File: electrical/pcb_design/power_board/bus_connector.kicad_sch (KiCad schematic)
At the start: 6 parts, among them J601 504050-1291, J603 504050-1091

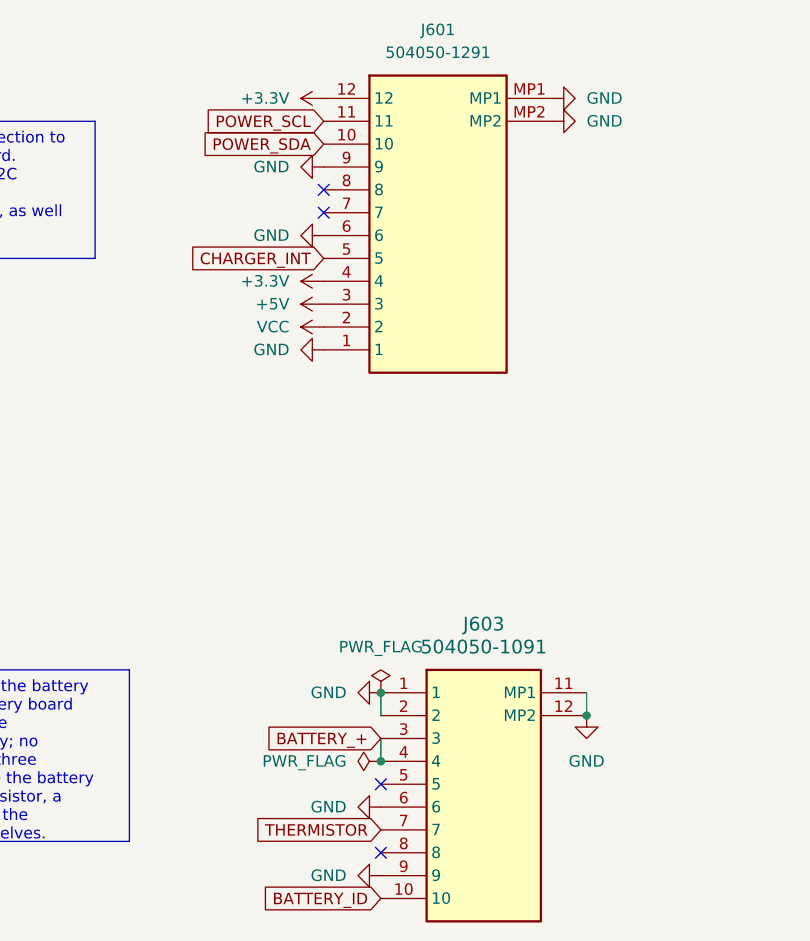
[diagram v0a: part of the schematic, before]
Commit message: Fixed major bug where header orientations need to be swapped on different ends of the cabling.
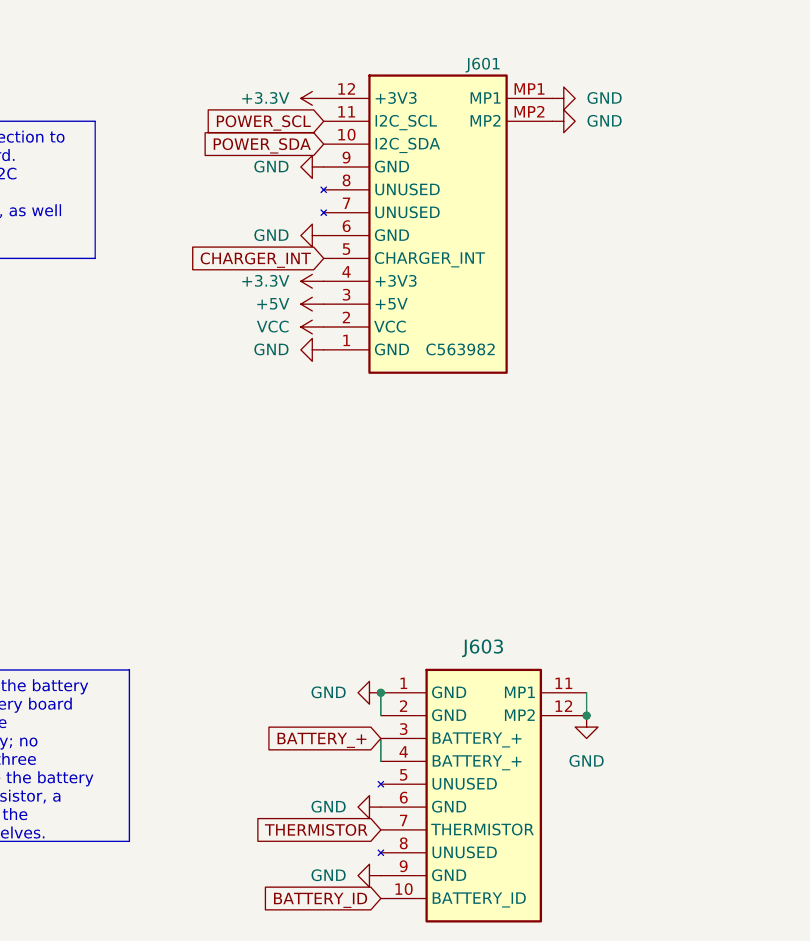
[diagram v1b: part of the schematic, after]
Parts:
- J601: value 504050-1291 -> Interconnect_Power_CPU-Power_side; symbol Molex 504050-1291:504050-1291 -> TVSC:Interconnect_Power_CPU-Power_side; Height 2.15 -> (none); Manufacturer MOLEX -> Molex; Manufacturer_Name Molex -> (none); Manufacturer_Part_Number 504050-1291 -> (none); Mouser Part Number 538-504050-1291 -> (none); Mouser Price/Stock https://www.mouser.co.uk/ProductDetail/Molex/504050-1291?qs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 -> (none)
- J603: value 504050-1091 -> Interconnect_Battery_Power-Power_side; symbol Molex 504050-1091:504050-1091 -> TVSC:Interconnect_Battery_Power-Power_side; Active Y -> (none); Manufacturer MOLEX -> Molex; Manufacturer_Name Molex -> (none); Manufacturer_Part_Number 504050-1091 -> (none); Mouser Part Number 538-504050-1091 -> (none); Mouser Price/Stock https://www.mouser.co.uk/ProductDetail/Molex/504050-1091?qs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 -> (none)
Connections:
- no-connect marks 4 -> 0
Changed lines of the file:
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@@
   (junction (at 201.93 95.25) (diameter 0) (color 0 0 0 0)
   )
-  (junction (at 121.92 128.27) (diameter 0) (color 0 0 0 0)
-  )
-  (no_connect (at 115.57 67.31))
-  (no_connect (at 115.57 64.77))
-  (no_connect (at 121.92 138.43))
-  (no_connect (at 121.92 130.81))
   (wire (pts (xy 144.78 120.65) (xy 144.78 123.19))
     (stroke (width 0) (type default))
@@
     )
   )
-  (symbol (lib_id "Molex 504050-1291:504050-1291") (at 115.57 54.61 0) (unit 1)
-    (in_bom yes) (on_board yes) (dnp no) (fields_autoplaced)
-    (property "Reference" "J601" (at 128.27 46.99 0)
-      (effects (font (size 1.27 1.27)))
-    )
-    (property "Value" "504050-1291" (at 128.27 49.53 0)
-      (effects (font (size 1.27 1.27)))
+  (symbol (lib_id "TVSC:Interconnect_Power_CPU-Power_side") (at 115.57 54.61 0) (unit 1)
+    (in_bom yes) (on_board yes) (dnp no)
+    (property "Reference" "J601" (at 133.35 50.8 0)
+      (effects (font (size 1.27 1.27)))
+    )
+    (property "Value" "Interconnect_Power_CPU-Power_side" (at 137.16 49.53 0)
+      (effects (font (size 1.27 1.27)) (justify left top) hide)
     )
     (property "Footprint" "footprints:5040501291" (at 137.16 149.53 0)
       (effects (font (size 1.27 1.27)) (justify left top) hide)
     )
-    (property "Datasheet" "" (at 137.16 249.53 0)
-      (effects (font (size 1.27 1.27)) (justify left top) hide)
-    )
-    (property "Height" "2.15" (at 137.16 449.53 0)
-      (effects (font (size 1.27 1.27)) (justify left top) hide)
-    )
-    (property "Manufacturer_Name" "Molex" (at 137.16 549.53 0)
-      (effects (font (size 1.27 1.27)) (justify left top) hide)
-    )
-    (property "Manufacturer_Part_Number" "504050-1291" (at 137.16 649.53 0)
-      (effects (font (size 1.27 1.27)) (justify left top) hide)
-    )
-    (property "Mouser Part Number" "538-504050-1291" (at 137.16 749.53 0)
-      (effects (font (size 1.27 1.27)) (justify left top) hide)
-    )
-    (property "Mouser Price/Stock" "https://www.mouser.co.uk/ProductDetail/Molex/504050-1291?qs=IvkZ4pJZlB2rki3iIhyJgg%3D%3D" (at 137.16 849.53 0)
-      (effects (font (size 1.27 1.27)) (justify left top) hide)
-    )
-    (property "Arrow Part Number" "" (at 137.16 949.53 0)
-      (effects (font (size 1.27 1.27)) (justify left top) hide)
-    )
-    (property "Arrow Price/Stock" "" (at 137.16 1049.53 0)
-      (effects (font (size 1.27 1.27)) (justify left top) hide)
-    )
-    (property "MPN" "C563982" (at 115.57 54.61 0)
-      (effects (font (size 1.27 1.27)) hide)
-    )
-    (property "Manufacturer" "MOLEX" (at 115.57 54.61 0)
-      (effects (font (size 1.27 1.27)) hide)
-    )
-    (property "Manufacturer Part Number" "504050-1291" (at 115.57 54.61 0)
-      (effects (font (size 1.27 1.27)) hide)
+    (property "Datasheet" "https://www.molex.com/en-us/products/part-detail/5040501291" (at 137.16 249.53 0)
+      (effects (font (size 1.27 1.27)) (justify left top) hide)
+    )
+    (property "MPN" "C563982" (at 130.81 82.55 0)
+      (effects (font (size 1.27 1.27)))
+    )
+    (property "Manufacturer" "Molex" (at 137.16 549.53 0)
+      (effects (font (size 1.27 1.27)) (justify left top) hide)
+    )
+    (property "Manufacturer Part Number" "504050-1291" (at 137.16 649.53 0)
+      (effects (font (size 1.27 1.27)) (justify left top) hide)
     )
     (property "Active" "Y" (at 115.57 54.61 0)
@@
     )
   )
-  (symbol (lib_id "power:PWR_FLAG") (at 121.92 128.27 90) (unit 1)
-    (in_bom yes) (on_board yes) (dnp no) (fields_autoplaced)
-    (property "Reference" "#FLG0602" (at 120.015 128.27 0)
-      (effects (font (size 1.27 1.27)) hide)
-    )
-    (property "Value" "PWR_FLAG" (at 118.11 128.27 90)
-      (effects (font (size 1.27 1.27)) (justify left))
-    )
-    (property "Footprint" "" (at 121.92 128.27 0)
-      (effects (font (size 1.27 1.27)) hide)
-    )
-    (property "Datasheet" "~" (at 121.92 128.27 0)
-      (effects (font (size 1.27 1.27)) hide)
-    )
-    (pin "1")
-    (instances
-      (project "power_board"
-        (path "/d7fbba2e-84c5-4e09-9d36-52dae726d12d/f5dda946-81da-4978-88f4-4ac2bc2b63d0"
-          (reference "#FLG0602") (unit 1)
-        )
-      )
-    )
-  )
-  (symbol (lib_id "power:PWR_FLAG") (at 121.92 120.65 0) (unit 1)
-    (in_bom yes) (on_board yes) (dnp no) (fields_autoplaced)
-    (property "Reference" "#FLG01" (at 121.92 118.745 0)
-      (effects (font (size 1.27 1.27)) hide)
-    )
-    (property "Value" "PWR_FLAG" (at 121.92 115.57 0)
-      (effects (font (size 1.27 1.27)))
-    )
-    (property "Footprint" "" (at 121.92 120.65 0)
-      (effects (font (size 1.27 1.27)) hide)
-    )
-    (property "Datasheet" "~" (at 121.92 120.65 0)
-      (effects (font (size 1.27 1.27)) hide)
-    )
-    (pin "1")
-    (instances
-      (project "power_board"
-        (path "/d7fbba2e-84c5-4e09-9d36-52dae726d12d/f5dda946-81da-4978-88f4-4ac2bc2b63d0"
-          (reference "#FLG01") (unit 1)
-        )
-      )
-    )
-  )
   (symbol (lib_id "power:GND") (at 201.93 104.14 0) (unit 1)
     (in_bom yes) (on_board yes) (dnp no) (fields_autoplaced)
@@
     )
   )
-  (symbol (lib_id "Molex 504050-1091:504050-1091") (at 121.92 120.65 0) (unit 1)
-    (in_bom yes) (on_board yes) (dnp no) (fields_autoplaced)
-    (property "Reference" "J603" (at 133.35 113.03 0)
+  (symbol (lib_id "TVSC:Interconnect_Battery_Power-Power_side") (at 121.92 120.65 0) (unit 1)
+    (in_bom yes) (on_board yes) (dnp no) (fields_autoplaced)
+    (property "Reference" "J603" (at 133.35 115.57 0)
       (effects (font (size 1.524 1.524)))
     )
-    (property "Value" "504050-1091" (at 133.35 115.57 0)
-      (effects (font (size 1.524 1.524)))
-    )
-    (property "Footprint" "footprints:504050-1091" (at 140.97 215.57 0)
-      (effects (font (size 1.27 1.27)) (justify left top) hide)
+    (property "Value" "Interconnect_Battery_Power-Power_side" (at 133.35 114.3 0)
+      (effects (font (size 1.27 1.27)) hide)
+    )
+    (property "Footprint" "footprints:504050-1091" (at 133.35 149.86 0)
+      (effects (font (size 1.27 1.27)) hide)
     )
     (property "Datasheet" "https://datasheet.datasheetarchive.com/originals/distributors/Datasheets_SAMA/78973205e9f4d17ddd54ea229574413e.pdf" (at 140.97 315.57 0)
       (effects (font (size 1.27 1.27)) (justify left top) hide)
     )
-    (property "MPN" "C5375652" (at 121.92 120.65 0)
-      (effects (font (size 1.27 1.27)) hide)
-    )
-    (property "Manufacturer" "MOLEX" (at 121.92 120.65 0)
-      (effects (font (size 1.27 1.27)) hide)
-    )
-    (property "Manufacturer Part Number" "504050-1091" (at 121.92 120.65 0)
-      (effects (font (size 1.27 1.27)) hide)
-    )
-    (property "Height" "" (at 140.97 515.57 0)
-      (effects (font (size 1.27 1.27)) (justify left top) hide)
-    )
-    (property "Manufacturer_Name" "Molex" (at 140.97 615.57 0)
-      (effects (font (size 1.27 1.27)) (justify left top) hide)
-    )
-    (property "Manufacturer_Part_Number" "504050-1091" (at 140.97 715.57 0)
-      (effects (font (size 1.27 1.27)) (justify left top) hide)
-    )
-    (property "Mouser Part Number" "538-504050-1091" (at 140.97 815.57 0)
-      (effects (font (size 1.27 1.27)) (justify left top) hide)
-    )
-    (property "Mouser Price/Stock" "https://www.mouser.co.uk/ProductDetail/Molex/504050-1091?qs=bvCPb%252BE7ys3Pdh2ki4M4Kw%3D%3D" (at 140.97 915.57 0)
-      (effects (font (size 1.27 1.27)) (justify left top) hide)
-    )
-    (property "Arrow Part Number" "" (at 140.97 1015.57 0)
-      (effects (font (size 1.27 1.27)) (justify left top) hide)
-    )
-    (property "Arrow Price/Stock" "" (at 140.97 1115.57 0)
-      (effects (font (size 1.27 1.27)) (justify left top) hide)
-    )
-    (property "Active" "Y" (at 121.92 120.65 0)
-      (effects (font (size 1.27 1.27)) hide)
+    (property "MPN" "C5375652" (at 139.7 147.32 0)
+      (effects (font (size 1.27 1.27)) (justify right) hide)
+    )
+    (property "Manufacturer" "Molex" (at 140.97 615.57 0)
+      (effects (font (size 1.27 1.27)) (justify left top) hide)
+    )
+    (property "Manufacturer Part Number" "504050-1091" (at 140.97 715.57 0)
+      (effects (font (size 1.27 1.27)) (justify left top) hide)
     )
     (pin "8")

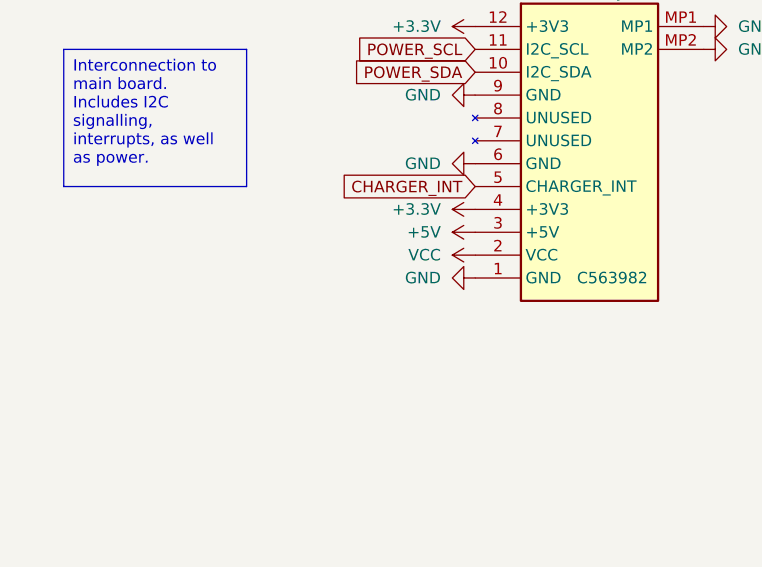
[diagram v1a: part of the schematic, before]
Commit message: Changed power indicator LEDs. Removed diodes from voltage regulators. Added a schottky diode to the VCC path to prevent misbehaving parts downstream from affecting the power board.
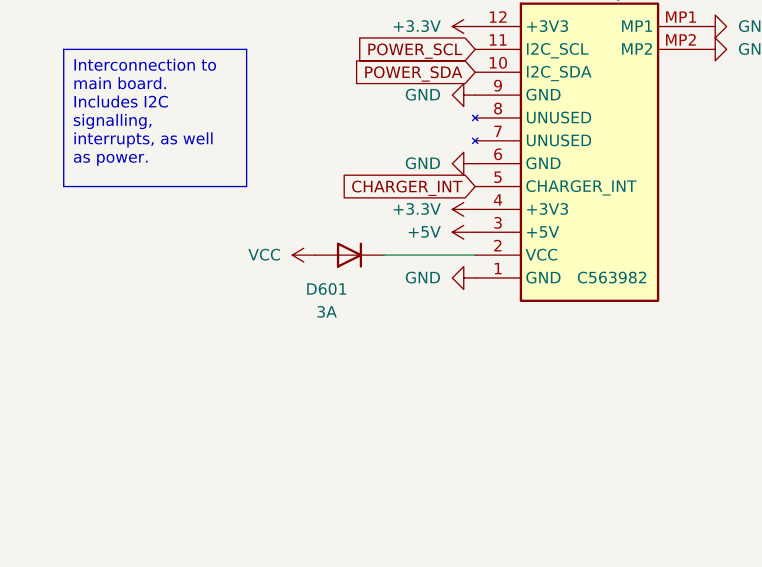
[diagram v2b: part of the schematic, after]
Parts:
- added D601: 3A, Diode_SMD:D_SOD-323, symbol Diode:1N4001
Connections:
- net VCC: now also D601.2 (A); no longer J601.2 (VCC)
- new net: D601.1 (K), J601.2 (VCC)
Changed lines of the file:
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@@
+    (stroke (width 0) (type default))
+  )
+  (wire (pts (xy 105.41 80.01) (xy 115.57 80.01))
     (stroke (width 0) (type default))
   )
@@
     )
   )
+  (symbol (lib_id "Diode:1N4001") (at 101.6 80.01 180) (unit 1)
+    (in_bom yes) (on_board yes) (dnp no)
+    (property "Reference" "D601" (at 99.06 83.82 0)
+      (effects (font (size 1.27 1.27)))
+    )
+    (property "Value" "3A" (at 99.06 86.36 0)
+      (effects (font (size 1.27 1.27)))
+    )
+    (property "Footprint" "Diode_SMD:D_SOD-323" (at 101.6 80.01 0)
+      (effects (font (size 1.27 1.27)) hide)
+    )
+    (property "Datasheet" "https://octopart.com/datasheet/b5818ws-tp-mcc-19245053" (at 101.6 80.01 0)
+      (effects (font (size 1.27 1.27)) hide)
+    )
+    (property "MPN" "C668861" (at 101.6 80.01 0)
+      (effects (font (size 1.27 1.27)) hide)
+    )
+    (property "Manufacturer" "MCC(Micro Commercial Components)" (at 101.6 80.01 0)
+      (effects (font (size 1.27 1.27)) hide)
+    )
+    (property "Manufacturer Part Number" "B5818WS-TP" (at 101.6 80.01 0)
+      (effects (font (size 1.27 1.27)) hide)
+    )
+    (property "Active" "Y" (at 101.6 80.01 0)
+      (effects (font (size 1.27 1.27)) hide)
+    )
+    (pin "2")
+    (pin "1")
+    (instances
+      (project "power_board"
+        (path "/d7fbba2e-84c5-4e09-9d36-52dae726d12d/f5dda946-81da-4978-88f4-4ac2bc2b63d0"
+          (reference "D601") (unit 1)
+        )
+      )
+    )
+  )
   (symbol (lib_id "power:GND") (at 115.57 62.23 270) (unit 1)
     (in_bom yes) (on_board yes) (dnp no) (fields_autoplaced)
@@
     )
   )
-  (symbol (lib_id "power:VCC") (at 115.57 80.01 90) (unit 1)
-    (in_bom yes) (on_board yes) (dnp no) (fields_autoplaced)
-    (property "Reference" "#PWR0607" (at 119.38 80.01 0)
-      (effects (font (size 1.27 1.27)) hide)
-    )
-    (property "Value" "VCC" (at 111.76 80.01 90)
+  (symbol (lib_id "power:VCC") (at 97.79 80.01 90) (unit 1)
+    (in_bom yes) (on_board yes) (dnp no) (fields_autoplaced)
+    (property "Reference" "#PWR07" (at 101.6 80.01 0)
+      (effects (font (size 1.27 1.27)) hide)
+    )
+    (property "Value" "VCC" (at 93.98 80.01 90)
       (effects (font (size 1.27 1.27)) (justify left))
     )
-    (property "Footprint" "" (at 115.57 80.01 0)
-      (effects (font (size 1.27 1.27)) hide)
-    )
-    (property "Datasheet" "" (at 115.57 80.01 0)
-      (effects (font (size 1.27 1.27)) hide)
-    )
-    (pin "1")
-    (instances
-      (project "power_board"
-        (path "/d7fbba2e-84c5-4e09-9d36-52dae726d12d/f5dda946-81da-4978-88f4-4ac2bc2b63d0"
-          (reference "#PWR0607") (unit 1)
-        )
-      )
+    (property "Footprint" "" (at 97.79 80.01 0)
+      (effects (font (size 1.27 1.27)) hide)
+    )
+    (property "Datasheet" "" (at 97.79 80.01 0)
+      (effects (font (size 1.27 1.27)) hide)
+    )
+    (pin "1")
+    (instances
+      (project "power_board"
+        (path "/d7fbba2e-84c5-4e09-9d36-52dae726d12d/f5dda946-81da-4978-88f4-4ac2bc2b63d0"
+          (reference "#PWR07") (unit 1)
+        )
+      )
